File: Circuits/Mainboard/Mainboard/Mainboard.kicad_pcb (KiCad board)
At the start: 2 copper layers, 13.5 x 1.1 mm, 26 parts, among them IC1 LM74500QDDFRQ1, IC2 LM74500QDDFRQ1, IC3 WSEN-ISDS 6-Dof IMU, IC4 SX1280IMLTRT, IC5 SKY66122-11, J1 XT60PW-M, J2 XT60PW-M, Q1 PSMN6R7-40MLDX, Q2 PSMN6R7-40MLDX, U1 NUCLEOH723ZG

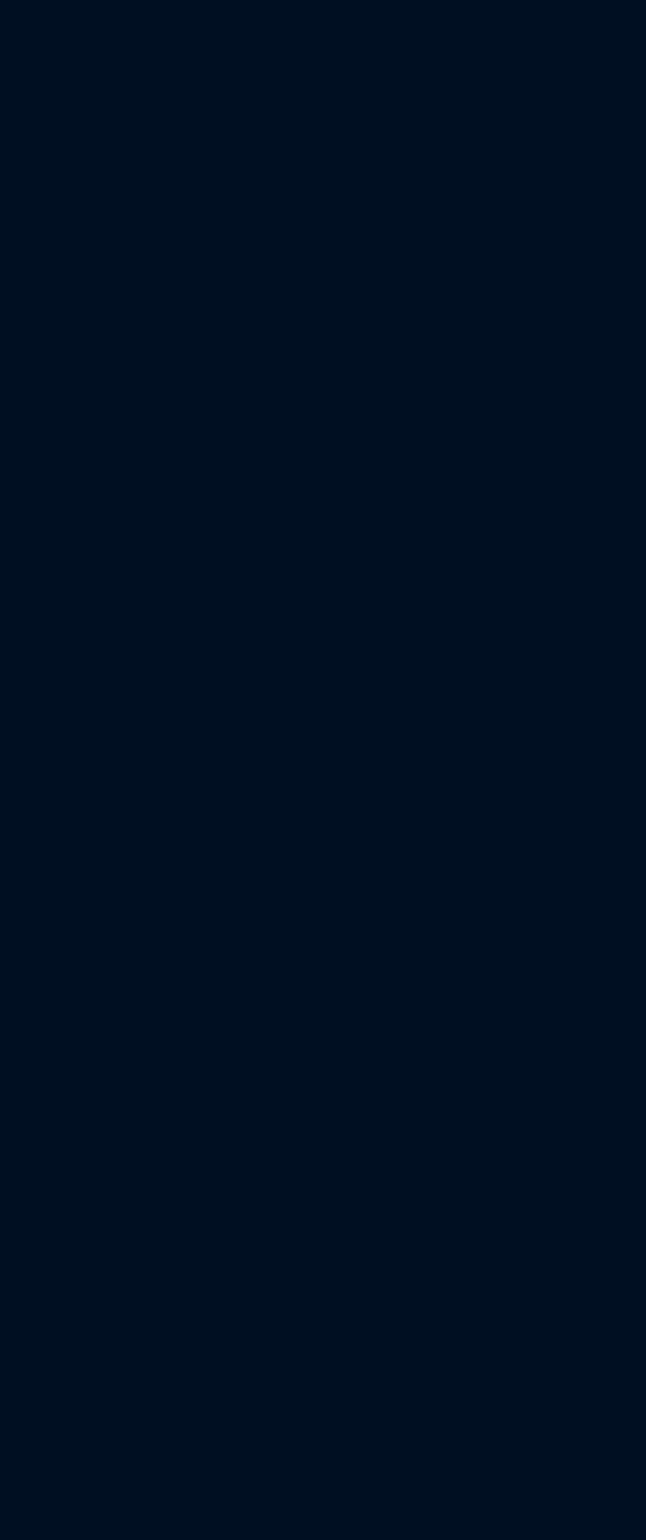
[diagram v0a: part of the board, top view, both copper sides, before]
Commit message: Added headers in the circuit for the mainboard in kicad
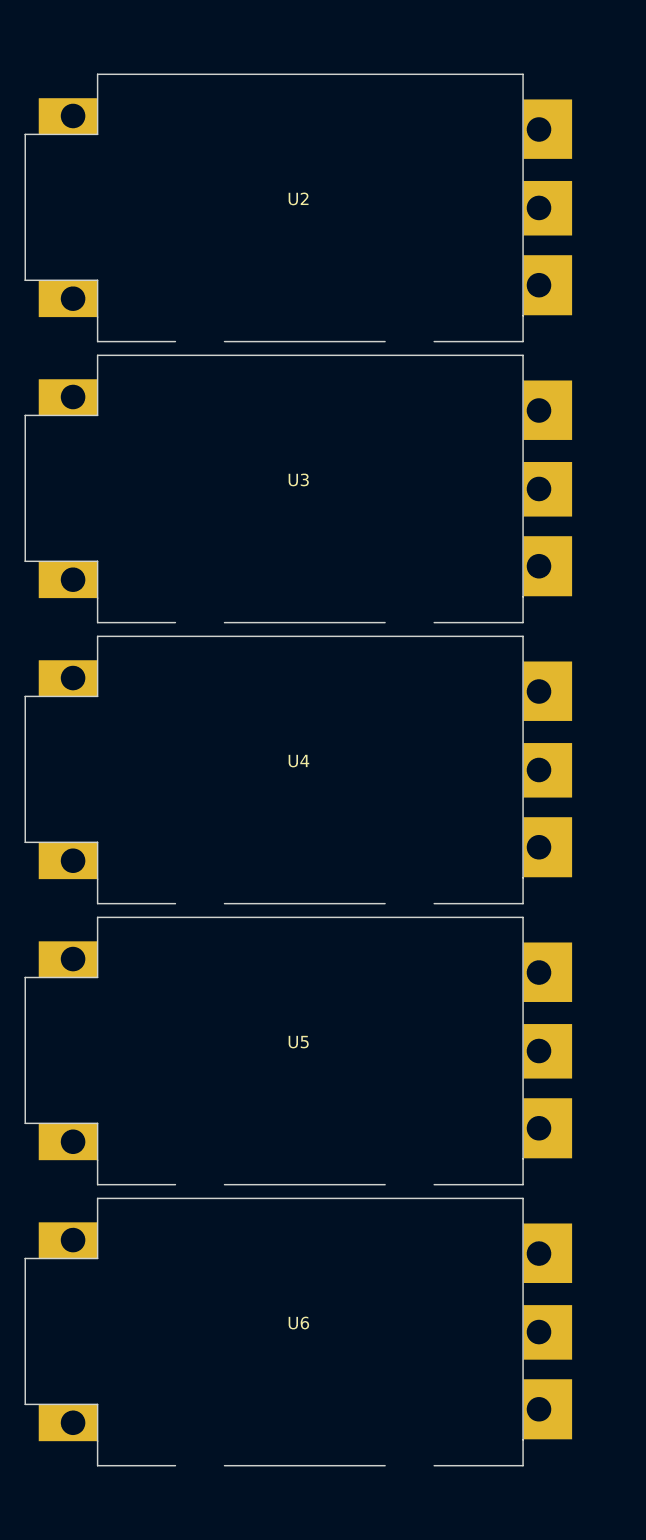
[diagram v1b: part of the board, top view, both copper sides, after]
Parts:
- added U2: B-G431B-ESC1, B-G431B-ESC1:B-G431B-ESC1_MOUNT, F.Cu at (50.4, 49.2)
- added U3: B-G431B-ESC1, B-G431B-ESC1:B-G431B-ESC1_MOUNT, F.Cu at (50.4, 72.2)
- added U4: B-G431B-ESC1, B-G431B-ESC1:B-G431B-ESC1_MOUNT, F.Cu at (50.4, 95.1)
- added U5: B-G431B-ESC1, B-G431B-ESC1:B-G431B-ESC1_MOUNT, F.Cu at (50.4, 118.0)
- added U6: B-G431B-ESC1, B-G431B-ESC1:B-G431B-ESC1_MOUNT, F.Cu at (50.4, 140.9)
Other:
- board size 13.5 x 1.1 mm -> 40.6 x 21.8 mm

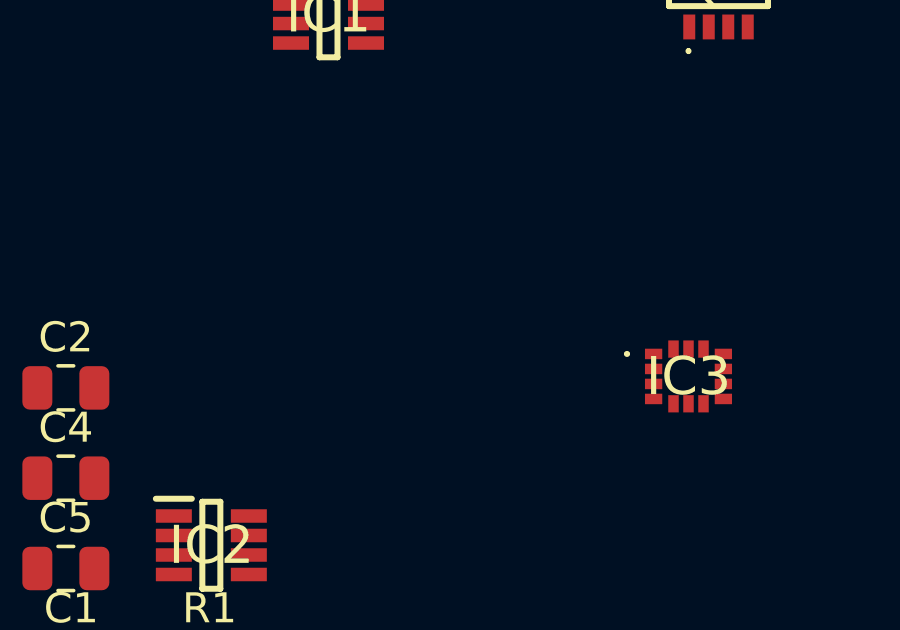
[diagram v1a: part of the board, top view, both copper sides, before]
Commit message: Removed unused components and added the rest of the nucleo to kicad schematic
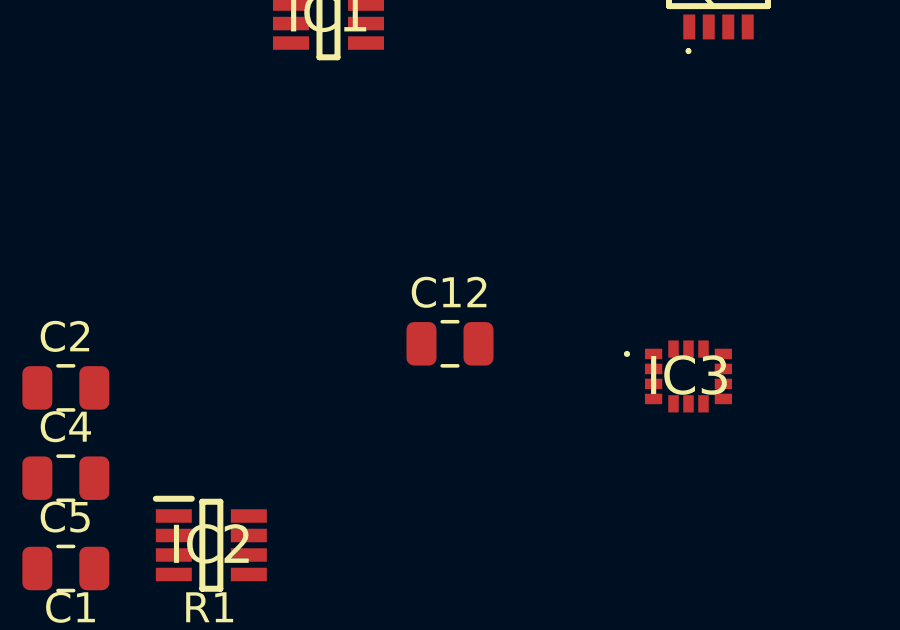
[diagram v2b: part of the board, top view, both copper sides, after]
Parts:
- added C12: 0.1uF, Capacitor_SMD:C_0805_2012Metric, F.Cu at (172.1, 61.5)
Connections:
- U1 pad CN10_1: (no net) -> unconnected-(U1F-AVDD-PadCN10_1)
- U1 pad CN10_10: (no net) -> unconnected-(U1F-D3/TIMER_A_PWM3-PadCN10_10)
- U1 pad CN10_11: (no net) -> unconnected-(U1F-A8/ADC_C_IN-PadCN10_11)
- U1 pad CN10_12: (no net) -> unconnected-(U1F-D2/IO-PadCN10_12)
- U1 pad CN10_13: (no net) -> unconnected-(U1F-D26/QSPI_CS-PadCN10_13)
- U1 pad CN10_14: (no net) -> unconnected-(U1F-D1/USART_A_TX-PadCN10_14)
- U1 pad CN10_15: (no net) -> unconnected-(U1F-D27/QSPI_CLK-PadCN10_15)
- U1 pad CN10_16: (no net) -> unconnected-(U1F-D0/USART_A_RX-PadCN10_16)
- U1 pad CN10_17: (no net) -> Net-(U1F-GND_CN10-PadCN10_17)
- U1 pad CN10_18: (no net) -> unconnected-(U1F-D42/TIMER_A_PWM1N-PadCN10_18)
- U1 pad CN10_19: (no net) -> unconnected-(U1F-D28/QSPI_BK1_IO3-PadCN10_19)
- U1 pad CN10_2: (no net) -> unconnected-(U1F-D7/IO-PadCN10_2)
- U1 pad CN10_20: (no net) -> unconnected-(U1F-D41/TIMER_A_ETR-PadCN10_20)
- U1 pad CN10_21: (no net) -> unconnected-(U1F-D29/QSPI_BK1_IO1-PadCN10_21)
- U1 pad CN10_22: (no net) -> Net-(U1F-GND_CN10-PadCN10_17)
- U1 pad CN10_23: (no net) -> unconnected-(U1F-D30/QSPI_BK1_IO0-PadCN10_23)
- U1 pad CN10_24: (no net) -> unconnected-(U1F-D40/TIMER_A_PWM2N-PadCN10_24)
- U1 pad CN10_25: (no net) -> unconnected-(U1F-D31/QSPI_BK1_IO2-PadCN10_25)
- U1 pad CN10_26: (no net) -> unconnected-(U1F-D39/TIMER_A_PWM3N-PadCN10_26)
- U1 pad CN10_27: (no net) -> Net-(U1F-GND_CN10-PadCN10_17)
- U1 pad CN10_28: (no net) -> unconnected-(U1F-D38/TIMER_A_BKIN2-PadCN10_28)
- U1 pad CN10_29: (no net) -> unconnected-(U1F-D32/TIMER_C_PWM1-PadCN10_29)
- U1 pad CN10_3: (no net) -> unconnected-(U1F-AGND_CN10-PadCN10_3)
- U1 pad CN10_30: (no net) -> unconnected-(U1F-D37/TIMER_A_BKIN1-PadCN10_30)
- U1 pad CN10_31: (no net) -> unconnected-(U1F-D33/TIMER_D_PWM1-PadCN10_31)
- U1 pad CN10_32: (no net) -> unconnected-(U1F-D36/TIMER_C_PWM2-PadCN10_32)
- U1 pad CN10_33: (no net) -> unconnected-(U1F-D34/TIMER_B_ETR-PadCN10_33)
- U1 pad CN10_34: (no net) -> unconnected-(U1F-D35/TIMER_C_PWM3-PadCN10_34)
- U1 pad CN10_4: (no net) -> unconnected-(U1F-D6/TIMER_A_PWM1-PadCN10_4)
- U1 pad CN10_5: (no net) -> Net-(U1F-GND_CN10-PadCN10_17)
- U1 pad CN10_6: (no net) -> unconnected-(U1F-D5/TIMER_A_PWM2-PadCN10_6)
- U1 pad CN10_7: (no net) -> unconnected-(U1F-A6/ADC_A_IN-PadCN10_7)
- U1 pad CN10_8: (no net) -> unconnected-(U1F-D4/IO-PadCN10_8)
- U1 pad CN10_9: (no net) -> unconnected-(U1F-A7/ADC_B_IN-PadCN10_9)
- U1 pad CN11_16: unconnected-(U1A-3V3-PadCN11_16) -> /3.3V
- U1 pad CN11_19: Net-(U1A-GND_CN11-PadCN11_19) -> GND
- U1 pad CN11_20: Net-(U1A-GND_CN11-PadCN11_19) -> GND
- U1 pad CN11_22: Net-(U1A-GND_CN11-PadCN11_19) -> GND
- U1 pad CN11_49: Net-(U1A-GND_CN11-PadCN11_19) -> GND
- U1 pad CN11_60: Net-(U1A-GND_CN11-PadCN11_19) -> GND
- U1 pad CN11_8: Net-(U1A-GND_CN11-PadCN11_19) -> GND
- U1 pad CN12_1: (no net) -> unconnected-(U1B-PC9-PadCN12_1)
- U1 pad CN12_10: (no net) -> unconnected-(U1B-PD8-PadCN12_10)
- U1 pad CN12_11: (no net) -> unconnected-(U1B-PA5-PadCN12_11)
- U1 pad CN12_12: (no net) -> unconnected-(U1B-PA12-PadCN12_12)
- U1 pad CN12_13: (no net) -> unconnected-(U1B-PA6-PadCN12_13)
- U1 pad CN12_14: (no net) -> unconnected-(U1B-PA11-PadCN12_14)
- U1 pad CN12_15: (no net) -> unconnected-(U1B-PA7-PadCN12_15)
- U1 pad CN12_16: (no net) -> unconnected-(U1B-PB12-PadCN12_16)
- U1 pad CN12_17: (no net) -> unconnected-(U1B-PB6-PadCN12_17)
- U1 pad CN12_18: (no net) -> unconnected-(U1B-PB11-PadCN12_18)
- U1 pad CN12_19: (no net) -> unconnected-(U1B-PC7-PadCN12_19)
- U1 pad CN12_2: (no net) -> unconnected-(U1B-PC8-PadCN12_2)
- U1 pad CN12_20: (no net) -> Net-(U1B-GND_CN12-PadCN12_20)
- U1 pad CN12_21: (no net) -> unconnected-(U1B-PA9-PadCN12_21)
- U1 pad CN12_22: (no net) -> unconnected-(U1B-PB2-PadCN12_22)
- U1 pad CN12_23: (no net) -> unconnected-(U1B-PA8-PadCN12_23)
- U1 pad CN12_24: (no net) -> unconnected-(U1B-PB1-PadCN12_24)
- U1 pad CN12_25: (no net) -> unconnected-(U1B-PB10-PadCN12_25)
- U1 pad CN12_26: (no net) -> unconnected-(U1B-PB15-PadCN12_26)
- U1 pad CN12_27: (no net) -> unconnected-(U1B-PB4-PadCN12_27)
- U1 pad CN12_28: (no net) -> unconnected-(U1B-PB14-PadCN12_28)
- U1 pad CN12_29: (no net) -> unconnected-(U1B-PB5-PadCN12_29)
- U1 pad CN12_3: (no net) -> unconnected-(U1B-PB8-PadCN12_3)
- U1 pad CN12_30: (no net) -> unconnected-(U1B-PB13-PadCN12_30)
- U1 pad CN12_31: (no net) -> unconnected-(U1B-PB3-PadCN12_31)
- U1 pad CN12_32: (no net) -> unconnected-(U1B-AGND_CN12-PadCN12_32)
- U1 pad CN12_33: (no net) -> unconnected-(U1B-PA10-PadCN12_33)
- U1 pad CN12_34: (no net) -> unconnected-(U1B-PC4-PadCN12_34)
- U1 pad CN12_35: (no net) -> unconnected-(U1B-PA2-PadCN12_35)
- U1 pad CN12_36: (no net) -> unconnected-(U1B-PF5-PadCN12_36)
- U1 pad CN12_37: (no net) -> unconnected-(U1B-PA3-PadCN12_37)
- U1 pad CN12_38: (no net) -> unconnected-(U1B-PF4-PadCN12_38)
- U1 pad CN12_39: (no net) -> Net-(U1B-GND_CN12-PadCN12_20)
- U1 pad CN12_4: (no net) -> unconnected-(U1B-PC6-PadCN12_4)
- U1 pad CN12_40: (no net) -> unconnected-(U1B-PE8-PadCN12_40)
- U1 pad CN12_41: (no net) -> unconnected-(U1B-PD13-PadCN12_41)
- U1 pad CN12_42: (no net) -> unconnected-(U1B-PF10-PadCN12_42)
- U1 pad CN12_43: (no net) -> unconnected-(U1B-PD12-PadCN12_43)
- U1 pad CN12_44: (no net) -> unconnected-(U1B-PE7-PadCN12_44)
- U1 pad CN12_45: (no net) -> unconnected-(U1B-PD11-PadCN12_45)
- U1 pad CN12_46: (no net) -> unconnected-(U1B-PD14-PadCN12_46)
- U1 pad CN12_47: (no net) -> unconnected-(U1B-PE10-PadCN12_47)
- U1 pad CN12_48: (no net) -> unconnected-(U1B-PD15-PadCN12_48)
- U1 pad CN12_49: (no net) -> unconnected-(U1B-PE12-PadCN12_49)
- U1 pad CN12_5: (no net) -> unconnected-(U1B-PB9-PadCN12_5)
- U1 pad CN12_50: (no net) -> unconnected-(U1B-PF14-PadCN12_50)
- U1 pad CN12_51: (no net) -> unconnected-(U1B-PE14-PadCN12_51)
- U1 pad CN12_52: (no net) -> unconnected-(U1B-PE9-PadCN12_52)
- U1 pad CN12_53: (no net) -> unconnected-(U1B-PE15-PadCN12_53)
- U1 pad CN12_54: (no net) -> Net-(U1B-GND_CN12-PadCN12_20)
- U1 pad CN12_55: (no net) -> unconnected-(U1B-PE13-PadCN12_55)
- U1 pad CN12_56: (no net) -> unconnected-(U1B-PE11-PadCN12_56)
- U1 pad CN12_57: (no net) -> unconnected-(U1B-PF13-PadCN12_57)
- U1 pad CN12_58: (no net) -> unconnected-(U1B-PF3-PadCN12_58)
- U1 pad CN12_59: (no net) -> unconnected-(U1B-PF12-PadCN12_59)
- U1 pad CN12_6: (no net) -> unconnected-(U1B-PC5-PadCN12_6)
- U1 pad CN12_60: (no net) -> unconnected-(U1B-PF15-PadCN12_60)
- U1 pad CN12_61: (no net) -> unconnected-(U1B-PG14-PadCN12_61)
- U1 pad CN12_62: (no net) -> unconnected-(U1B-PF11-PadCN12_62)
- U1 pad CN12_63: (no net) -> Net-(U1B-GND_CN12-PadCN12_20)
- U1 pad CN12_64: (no net) -> unconnected-(U1B-PE0-PadCN12_64)
- U1 pad CN12_65: (no net) -> unconnected-(U1B-PD10-PadCN12_65)
- U1 pad CN12_66: (no net) -> unconnected-(U1B-PG8-PadCN12_66)
- U1 pad CN12_67: (no net) -> unconnected-(U1B-PG7-PadCN12_67)
- U1 pad CN12_68: (no net) -> unconnected-(U1B-PG5-PadCN12_68)
- U1 pad CN12_69: (no net) -> unconnected-(U1B-PG4-PadCN12_69)
- U1 pad CN12_7: (no net) -> unconnected-(U1B-VREFP-PadCN12_7)
- U1 pad CN12_70: (no net) -> unconnected-(U1B-PG6-PadCN12_70)
- U1 pad CN12_8: (no net) -> unconnected-(U1B-5V_USB_STLK-PadCN12_8)
- U1 pad CN12_9: (no net) -> Net-(U1B-GND_CN12-PadCN12_20)
- U1 pad CN15_1: (no net) -> Net-(U1I-GND_CN15-PadCN15_1)
- U1 pad CN15_2: (no net) -> Net-(U1I-GND_CN15-PadCN15_1)
- U1 pad CN16_1: (no net) -> Net-(U1J-GND_CN16-PadCN16_1)
- U1 pad CN16_2: (no net) -> Net-(U1J-GND_CN16-PadCN16_1)
- U1 pad CN3_1: (no net) -> Net-(U1G-GND_CN3-PadCN3_1)
- U1 pad CN3_2: (no net) -> Net-(U1G-GND_CN3-PadCN3_1)
- U1 pad CN4_1: (no net) -> Net-(U1H-GND_CN4-PadCN4_1)
- U1 pad CN4_2: (no net) -> Net-(U1H-GND_CN4-PadCN4_1)
- U1 pad CN7_1: (no net) -> unconnected-(U1E-D16/I2S_A_MCK-PadCN7_1)
- U1 pad CN7_10: (no net) -> unconnected-(U1E-D13/SPI_A_SCK-PadCN7_10)
- U1 pad CN7_11: (no net) -> unconnected-(U1E-D21/I2S_B_MCK-PadCN7_11)
- U1 pad CN7_12: (no net) -> unconnected-(U1E-D12/SPI_A_MISO-PadCN7_12)
- U1 pad CN7_13: (no net) -> unconnected-(U1E-D22/I2S_B_SD/SPI_B_MOSI-PadCN7_13)
- U1 pad CN7_14: (no net) -> unconnected-(U1E-D11/SPI_A_MOSI/TIM_E_PWM1-PadCN7_14)
- U1 pad CN7_15: (no net) -> unconnected-(U1E-D23/I2S_B_CK/SPI_B_SCK-PadCN7_15)
- U1 pad CN7_16: (no net) -> unconnected-(U1E-D10/SPI_A_CS/TIM_B_PWM3-PadCN7_16)
- U1 pad CN7_17: (no net) -> unconnected-(U1E-D24/SPI_B_NSS-PadCN7_17)
- U1 pad CN7_18: (no net) -> unconnected-(U1E-D9/TIMER_B_PWM2-PadCN7_18)
- U1 pad CN7_19: (no net) -> unconnected-(U1E-D25/SPI_B_MISO-PadCN7_19)
- U1 pad CN7_2: (no net) -> unconnected-(U1E-D15/I2C_A_SCL-PadCN7_2)
- U1 pad CN7_20: (no net) -> unconnected-(U1E-D8/IO-PadCN7_20)
- U1 pad CN7_3: (no net) -> unconnected-(U1E-D17/I2S_A_SD-PadCN7_3)
- U1 pad CN7_4: (no net) -> unconnected-(U1E-D14/I2C_A_SDA-PadCN7_4)
- U1 pad CN7_5: (no net) -> unconnected-(U1E-D18/I2S_A_CK-PadCN7_5)
- U1 pad CN7_6: (no net) -> unconnected-(U1E-VREFP_CN7-PadCN7_6)
- U1 pad CN7_7: (no net) -> unconnected-(U1E-D19/I2S_A_WS-PadCN7_7)
- U1 pad CN7_8: (no net) -> unconnected-(U1E-GND_CN7-PadCN7_8)
- U1 pad CN7_9: (no net) -> unconnected-(U1E-D20/I2S_B_WS-PadCN7_9)
- U1 pad CN8_1: (no net) -> unconnected-(U1C-NC_CN8-PadCN8_1)
- U1 pad CN8_10: (no net) -> unconnected-(U1C-D47/SDMMC_CK-PadCN8_10)
- U1 pad CN8_11: (no net) -> Net-(U1C-GND_CN8-PadCN8_11)
- U1 pad CN8_12: (no net) -> unconnected-(U1C-D48/SDMMC_CMD-PadCN8_12)
- U1 pad CN8_13: (no net) -> Net-(U1C-GND_CN8-PadCN8_11)
- U1 pad CN8_14: (no net) -> unconnected-(U1C-D49/IO-PadCN8_14)
- U1 pad CN8_15: (no net) -> unconnected-(U1C-VIN_CN8-PadCN8_15)
- U1 pad CN8_16: (no net) -> unconnected-(U1C-D50/IO-PadCN8_16)
- U1 pad CN8_2: (no net) -> unconnected-(U1C-D43/SDMMC_D0-PadCN8_2)
- U1 pad CN8_3: (no net) -> unconnected-(U1C-IOREF_CN8-PadCN8_3)
- U1 pad CN8_4: (no net) -> unconnected-(U1C-D44/SDMMC_D1/I2S_A_CKIN-PadCN8_4)
- U1 pad CN8_5: (no net) -> unconnected-(U1C-NRST_CN8-PadCN8_5)
- U1 pad CN8_6: (no net) -> unconnected-(U1C-D45/SDMMC_D2-PadCN8_6)
- U1 pad CN8_7: (no net) -> unconnected-(U1C-3V3_CN8-PadCN8_7)
- U1 pad CN8_8: (no net) -> unconnected-(U1C-D46/SDMMC_D3-PadCN8_8)
- U1 pad CN8_9: (no net) -> unconnected-(U1C-5V_CN8-PadCN8_9)
- U1 pad CN9_1: (no net) -> unconnected-(U1D-A0/ADC12_INP15-PadCN9_1)
- U1 pad CN9_10: (no net) -> unconnected-(U1D-D55/USART_B_CTS-PadCN9_10)
- U1 pad CN9_11: (no net) -> unconnected-(U1D-A5/ADC3_INP6/I2C1_SCL-PadCN9_11)
- U1 pad CN9_12: (no net) -> Net-(U1D-GND_CN9-PadCN9_12)
- U1 pad CN9_13: (no net) -> unconnected-(U1D-D72/COMP1_INP-PadCN9_13)
- U1 pad CN9_14: (no net) -> unconnected-(U1D-D56/SAI_A_MCLK-PadCN9_14)
- U1 pad CN9_15: (no net) -> unconnected-(U1D-D71/COMP2_INP-PadCN9_15)
- U1 pad CN9_16: (no net) -> unconnected-(U1D-D57/SAI_A_FS-PadCN9_16)
- U1 pad CN9_17: (no net) -> unconnected-(U1D-D70/I2C_B_SMBA-PadCN9_17)
- U1 pad CN9_18: (no net) -> unconnected-(U1D-D58/SAI_A_SCK-PadCN9_18)
- U1 pad CN9_19: (no net) -> unconnected-(U1D-D69/I2C_B_SCL-PadCN9_19)
- U1 pad CN9_2: (no net) -> unconnected-(U1D-D51/USART_B_SCLK-PadCN9_2)
- U1 pad CN9_20: (no net) -> unconnected-(U1D-D59/SAI_A_SD-PadCN9_20)
- U1 pad CN9_21: (no net) -> unconnected-(U1D-D68/I2C_B_SDA-PadCN9_21)
- U1 pad CN9_22: (no net) -> unconnected-(U1D-D60/SAI_B_SD-PadCN9_22)
- U1 pad CN9_23: (no net) -> Net-(U1D-GND_CN9-PadCN9_12)
- U1 pad CN9_24: (no net) -> unconnected-(U1D-D61/SAI_B_SCK-PadCN9_24)
- U1 pad CN9_25: (no net) -> unconnected-(U1D-D67/CAN_RX-PadCN9_25)
- U1 pad CN9_26: (no net) -> unconnected-(U1D-D62/SAI_B_MCLK-PadCN9_26)
- U1 pad CN9_27: (no net) -> unconnected-(U1D-D66/CAN_TX-PadCN9_27)
- U1 pad CN9_28: (no net) -> unconnected-(U1D-D63/SAI_B_FS-PadCN9_28)
- U1 pad CN9_29: (no net) -> unconnected-(U1D-D65/IO-PadCN9_29)
- U1 pad CN9_3: (no net) -> unconnected-(U1D-A1/ADC123_INP10-PadCN9_3)
- U1 pad CN9_30: (no net) -> unconnected-(U1D-D64/IO-PadCN9_30)
- U1 pad CN9_4: (no net) -> unconnected-(U1D-D52/USART_B_RX-PadCN9_4)
- U1 pad CN9_5: (no net) -> unconnected-(U1D-A2/ADC12_INP13-PadCN9_5)
- U1 pad CN9_6: (no net) -> unconnected-(U1D-D53/USART_B_TX-PadCN9_6)
- U1 pad CN9_7: (no net) -> unconnected-(U1D-A3/ADC12_INP5-PadCN9_7)
- U1 pad CN9_8: (no net) -> unconnected-(U1D-D54/USART_B_RTS-PadCN9_8)
- U1 pad CN9_9: (no net) -> unconnected-(U1D-A4/ADC123_INP12/I2C1_SDA-PadCN9_9)

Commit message: Added 3D models for the pcb components
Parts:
- removed U2, U3, U4, U5, U6: B-G431B-ESC1, B-G431B-ESC1:B-G431B-ESC1_MOUNT
- added C13: 0.1uF, Capacitor_SMD:C_0805_2012Metric, F.Cu at (244.2, 75.8)
- added C14: 0.1uF, Capacitor_SMD:C_0805_2012Metric, F.Cu at (247.3, 75.8)
- added C15: 100nF, Capacitor_SMD:C_0805_2012Metric, F.Cu at (250.3, 75.8)
- added C16: 1nF, Capacitor_SMD:C_0805_2012Metric, F.Cu at (253.3, 75.8)
- added C17: 100nF, Capacitor_SMD:C_0805_2012Metric, F.Cu at (256.3, 75.8)
- added C18: 1nF, Capacitor_SMD:C_0805_2012Metric, F.Cu at (259.3, 75.8)
- added C19: 1uF, Capacitor_SMD:C_0805_2012Metric, F.Cu at (244.2, 71.3)
- added C20: 10nF, Capacitor_SMD:C_0805_2012Metric, F.Cu at (247.3, 71.3)
- added C21: 10nF, Capacitor_SMD:C_0805_2012Metric, F.Cu at (250.3, 71.3)
- added C22: 470uF, Capacitor_SMD:C_0805_2012Metric, F.Cu at (253.3, 71.3)
- added C23: 0.1uF, Capacitor_SMD:C_0805_2012Metric, F.Cu at (256.3, 71.3)
- added IC6: TS2596CM533_RNG, TS2596CM533_RNG:TS2596CM550RNG, F.Cu at (204.4, 129.4)
- added J4: Conn_01x05_Pin, Connector_PinHeader_1.00mm:PinHeader_1x05_P1.00mm_Vertical, F.Cu at (269.4, 164.3)
- added J5: B6B-PH-K-S, B6B-PH-K-S:JST_B6B-PH-K-S, F.Cu at (261.5, 183.2)
- added J6: B5P-VH_LF__SN_, B5P-VH-LF-SN:B5P-VH_LF__SN_, F.Cu at (233.0, 180.4)
- added L2: AMRM00101040470MA1, AMRM00101040470MA1:AMRM00101040470MA1, F.Cu at (226.1, 51.8)
- moved J1 149.7 mm to (195.3, 172.4)
- moved J2 148.6 mm to (215.6, 172.4)
- moved Q2 133.0 mm to (219.0, 150.1)
- moved C2 120.0 mm to (219.1, 167.0)
- moved C4 114.5 mm to (219.1, 163.6)
- moved IC1 111.7 mm to (196.3, 158.6), turned to 90 degrees
- moved IC2 106.4 mm to (219.1, 159.2), turned to 90 degrees
- moved Q1 101.8 mm to (196.4, 150.0), turned to 180 degrees
- moved C1 101.8 mm to (196.3, 166.8)
- moved R2 96.9 mm to (218.9, 154.8)
- moved C3 95.9 mm to (196.3, 163.5)
- moved R1 88.3 mm to (196.3, 154.2)
- moved PS1 68.2 mm to (233.7, 149.8)
- moved C12 67.6 mm to (227.8, 99.8)
- moved C5 67.6 mm to (215.0, 107.2)
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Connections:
- C12 pad 1: /3.3V -> Net-(U1A-3V3)
- IC4 pad 1: unconnected-(IC4-VR_PA-Pad1) -> Net-(IC4-VR_PA)
- IC4 pad 12: unconnected-(IC4-DCC_FB-Pad12) -> Net-(IC4-DCC_FB)
- IC4 pad 13: unconnected-(IC4-GND_2-Pad13) -> GND
- IC4 pad 15: unconnected-(IC4-VBAT-Pad15) -> /3.3V
- IC4 pad 2: unconnected-(IC4-VDD_IN-Pad2) -> Net-(IC4-DCC_FB)
- IC4 pad 20: unconnected-(IC4-GND_3-Pad20) -> GND
- IC4 pad 21: unconnected-(IC4-GND_4-Pad21) -> GND
- IC4 pad 23: unconnected-(IC4-GND_5-Pad23) -> GND
- IC4 pad 24: unconnected-(IC4-GND_6-Pad24) -> GND
- IC4 pad 5: unconnected-(IC4-GND_1-Pad5) -> GND
- U1 pad CN10_17: Net-(U1F-GND_CN10-PadCN10_17) -> GND
- U1 pad CN10_22: Net-(U1F-GND_CN10-PadCN10_17) -> GND
- U1 pad CN10_27: Net-(U1F-GND_CN10-PadCN10_17) -> GND
- U1 pad CN10_5: Net-(U1F-GND_CN10-PadCN10_17) -> GND
- U1 pad CN11_16: /3.3V -> Net-(U1A-3V3)
- U1 pad CN12_20: Net-(U1B-GND_CN12-PadCN12_20) -> GND
- U1 pad CN12_32: unconnected-(U1B-AGND_CN12-PadCN12_32) -> GND
- U1 pad CN12_39: Net-(U1B-GND_CN12-PadCN12_20) -> GND
- U1 pad CN12_54: Net-(U1B-GND_CN12-PadCN12_20) -> GND
- U1 pad CN12_63: Net-(U1B-GND_CN12-PadCN12_20) -> GND
- U1 pad CN12_9: Net-(U1B-GND_CN12-PadCN12_20) -> GND
- U1 pad CN15_1: Net-(U1I-GND_CN15-PadCN15_1) -> GND
- U1 pad CN15_2: Net-(U1I-GND_CN15-PadCN15_1) -> GND
- U1 pad CN16_1: Net-(U1J-GND_CN16-PadCN16_1) -> GND
- U1 pad CN16_2: Net-(U1J-GND_CN16-PadCN16_1) -> GND
- U1 pad CN3_1: Net-(U1G-GND_CN3-PadCN3_1) -> GND
- U1 pad CN3_2: Net-(U1G-GND_CN3-PadCN3_1) -> GND
- U1 pad CN4_1: Net-(U1H-GND_CN4-PadCN4_1) -> GND
- U1 pad CN4_2: Net-(U1H-GND_CN4-PadCN4_1) -> GND
- U1 pad CN7_8: unconnected-(U1E-GND_CN7-PadCN7_8) -> GND
- U1 pad CN8_11: Net-(U1C-GND_CN8-PadCN8_11) -> GND
- U1 pad CN8_12: unconnected-(U1C-D48/SDMMC_CMD-PadCN8_12) -> GND
- U1 pad CN8_13: Net-(U1C-GND_CN8-PadCN8_11) -> GND
- U1 pad CN8_14: unconnected-(U1C-D49/IO-PadCN8_14) -> GND
- U1 pad CN8_7: unconnected-(U1C-3V3_CN8-PadCN8_7) -> /3.3V
- U1 pad CN8_8: unconnected-(U1C-D46/SDMMC_D3-PadCN8_8) -> /3.3V
- U1 pad CN9_12: Net-(U1D-GND_CN9-PadCN9_12) -> GND
- U1 pad CN9_23: Net-(U1D-GND_CN9-PadCN9_12) -> GND
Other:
- board size 40.6 x 21.8 mm -> 160 x 160 mm
